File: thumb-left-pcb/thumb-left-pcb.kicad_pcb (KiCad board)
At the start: 2 copper layers, 77 x 88 mm, 31 parts, among them J1 Conn_01x10

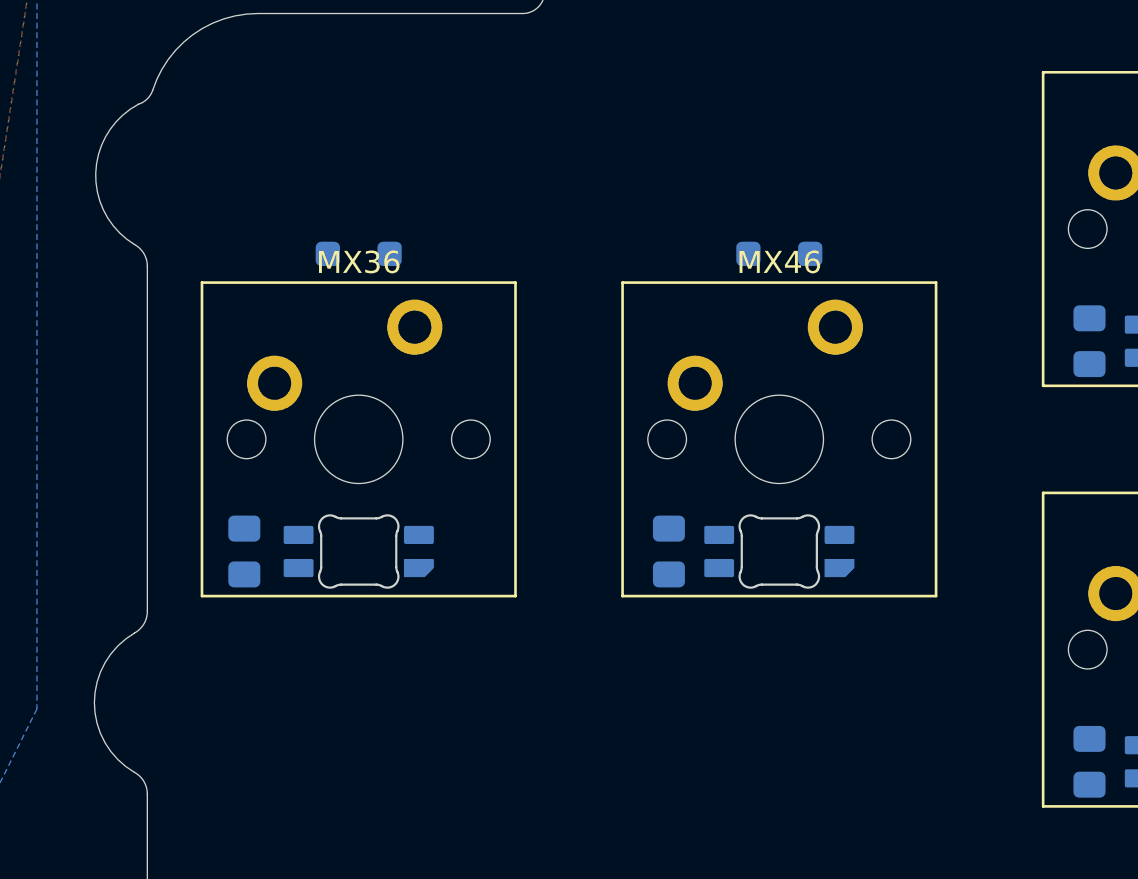
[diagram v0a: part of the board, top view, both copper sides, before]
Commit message: added 2u stabilizers
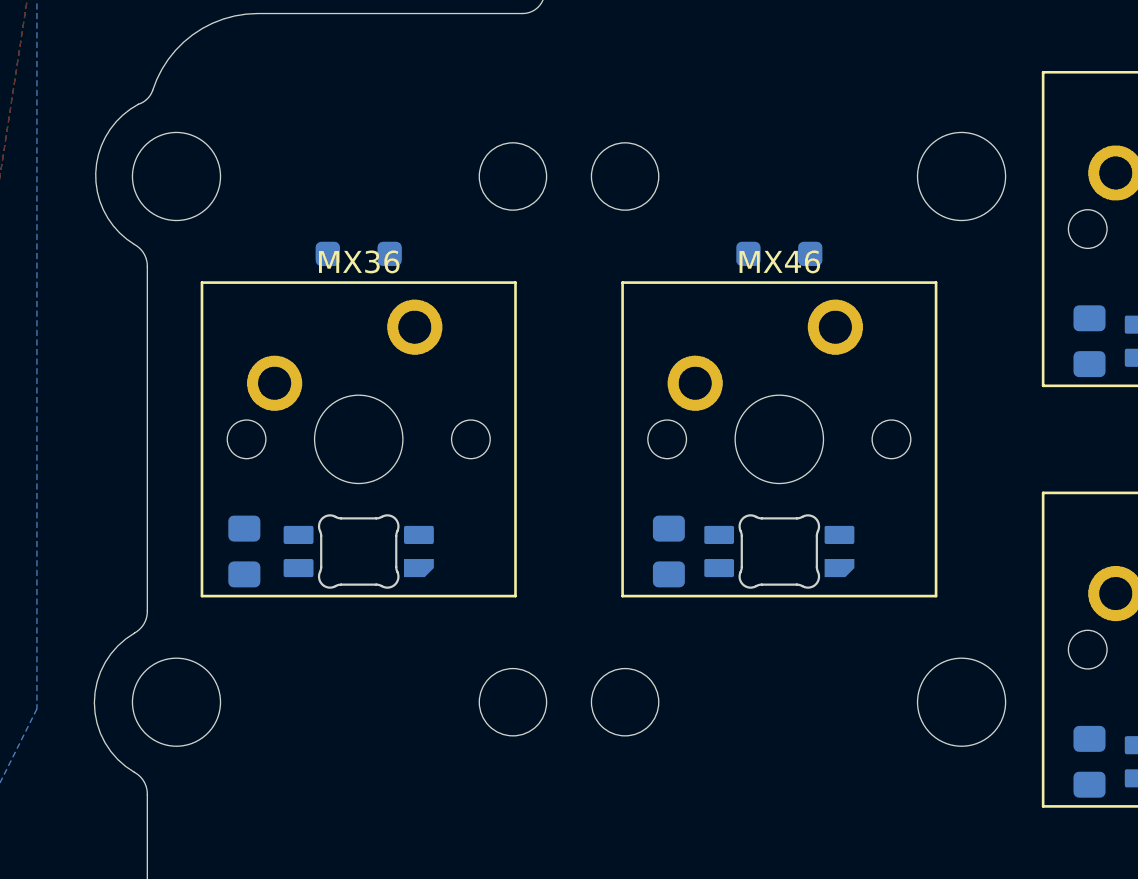
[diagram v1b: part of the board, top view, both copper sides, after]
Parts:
- added REF**: STAB_MX_2u, PCM_marbastlib-mx:STAB_MX_2u, F.Cu at (203.6, 77.8)
- added REF**: STAB_MX_2u, PCM_marbastlib-mx:STAB_MX_2u, F.Cu at (184.6, 77.8)

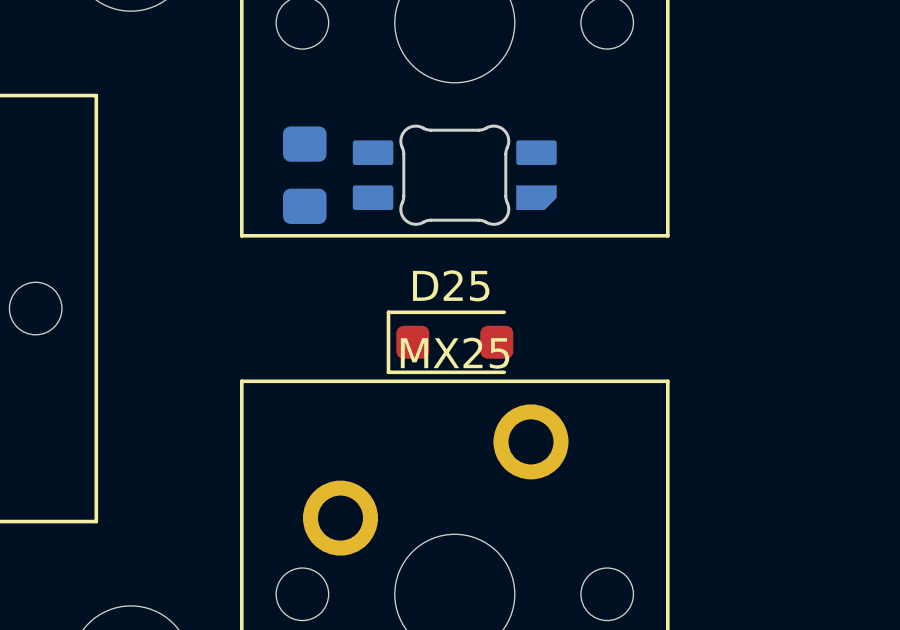
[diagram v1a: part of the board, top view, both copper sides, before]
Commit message: left D25 flipped
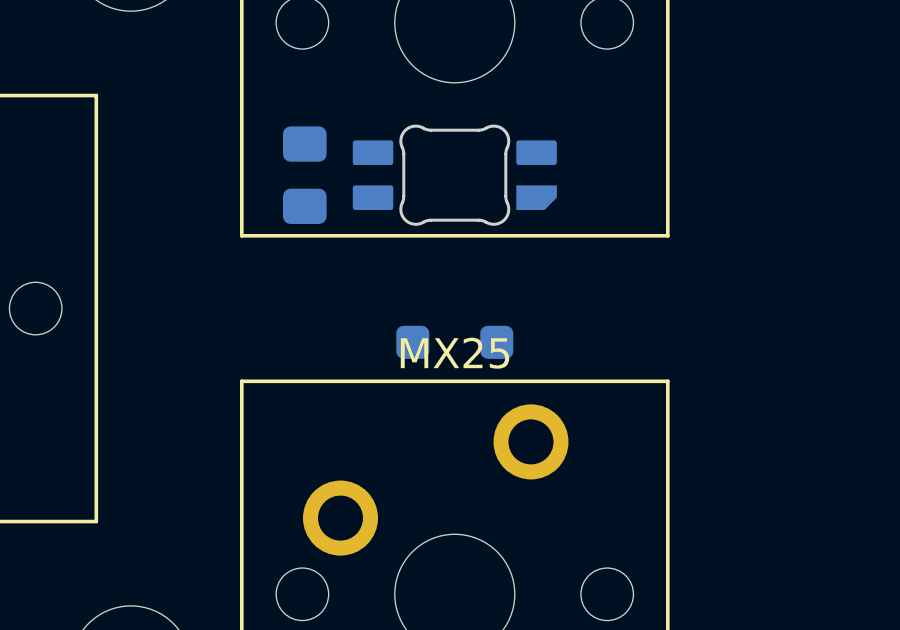
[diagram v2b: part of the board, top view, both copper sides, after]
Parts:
- D25: moved to B.Cu
- turned D25 to 180 degrees

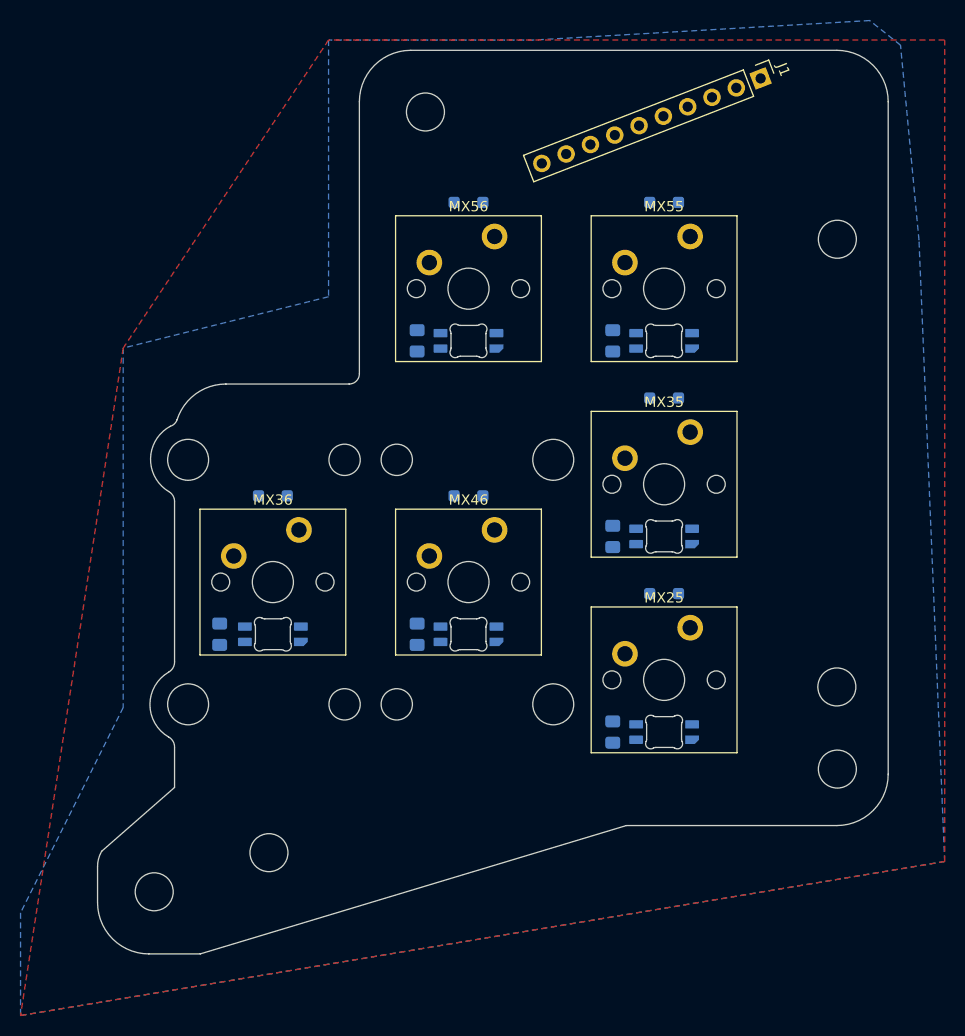
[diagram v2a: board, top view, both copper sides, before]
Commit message: left thumb routed
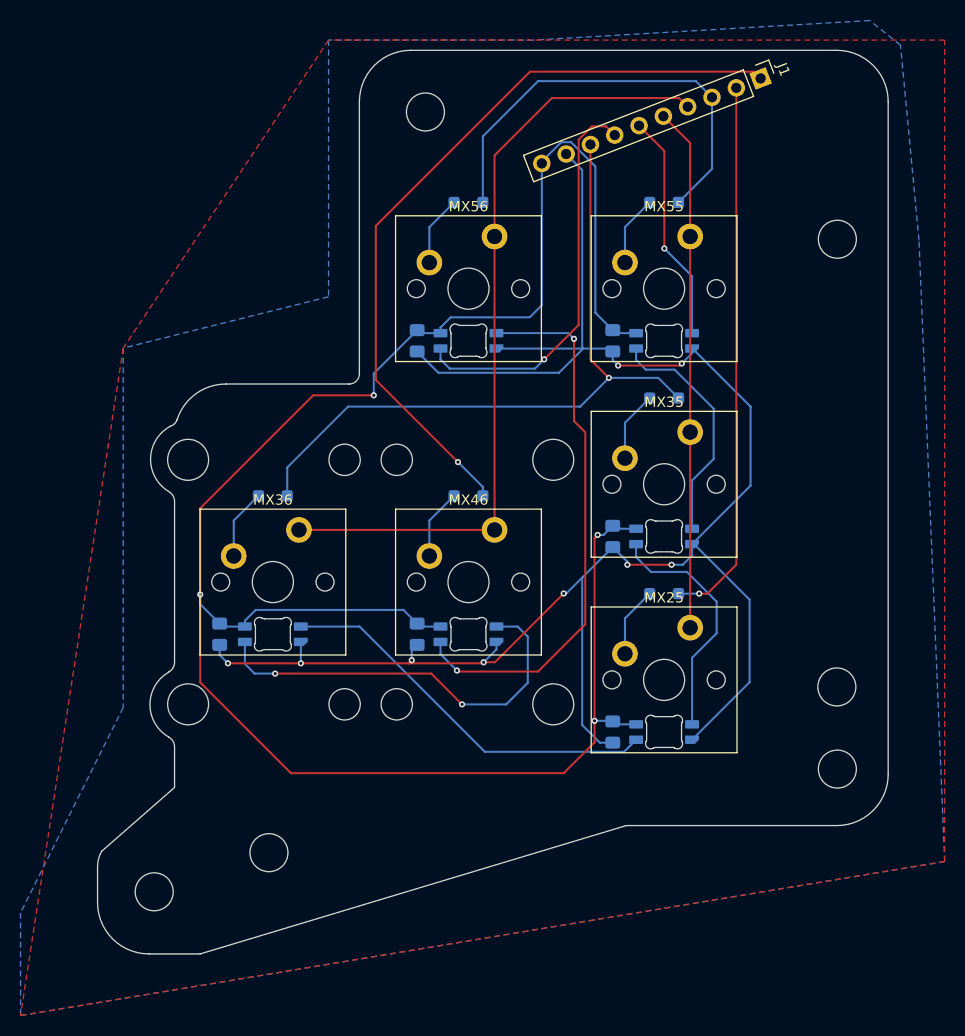
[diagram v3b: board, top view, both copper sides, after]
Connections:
- D55 pad 1: /COL_R6 -> /ROW_5
- D56 pad 1: /COL_R6 -> /ROW_5
- J1 pad 3: /COL_R6 -> /ROW_5
- J1 pad 4: /COL_6 -> /COL_L6
- J1 pad 5: /COL_5 -> /COL_L5
- MX25 pad 2: /COL_R5 -> /COL_L5
- MX35 pad 2: /COL_R5 -> /COL_L5
- MX36 pad 2: /COL_R6 -> /COL_L6
- MX46 pad 2: /COL_R6 -> /COL_L6
- MX55 pad 2: /COL_R5 -> /COL_L5
- MX56 pad 2: /COL_R6 -> /COL_L6
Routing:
- net /VDD: track 0.00 -> 199.2 mm, vias 0 -> 4
- net GND: track 0.00 -> 185.6 mm, vias 0 -> 9
- net /COL_L6: track 0.00 -> 77.0 mm
- net /ROW_4: track 0.00 -> 74.6 mm, vias 0 -> 1
- net /ROW_3: track 0.00 -> 68.8 mm, vias 0 -> 1
- net Net-(LED46-DOUT): track 0.00 -> 53.9 mm, vias 0 -> 2
- net /ROW_2: track 0.00 -> 53.2 mm, vias 0 -> 1
- net /COL_L5: track 0.00 -> 50.9 mm
- net /ROW_5: track 0.00 -> 43.2 mm
- net Net-(LED36-DOUT): track 0.00 -> 40.1 mm, vias 0 -> 2
- net /DOUT: track 0.00 -> 39.1 mm, vias 0 -> 1
- net Net-(LED25-DOUT): track 0.00 -> 38.2 mm
- net Net-(LED25-DIN): track 0.00 -> 23.8 mm
- net Net-(LED35-DIN): track 0.00 -> 23.2 mm
- net /DIN: track 0.00 -> 22.3 mm, vias 0 -> 1
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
